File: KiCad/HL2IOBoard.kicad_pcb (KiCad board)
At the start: 4 copper layers, 93 x 53.4 mm, 117 parts, among them J1 Conn_02x25_Odd_Even, J10 142-0701-851, J12 Conn_02x01, J2 Conn_01x05, J3 FAN, J4 Conn_02x04_Odd_Even, J5 LD09P13A4GX00LF, J6 Conn_02x04_Odd_Even, J7 Conn_01x09, J8 Conn_01x05, J9 142-0701-851, P1 TestPoint, P2 TestPoint, P3 TestPoint, P4 TestPoint, Q1 NUD3160LT1G, Q2 SSM3J374R,LF, Q3 SSM3J374R,LF, Q4 BC847C-13-F, Q5 BC847C-13-F, Q6 FCX491ATA, Sw12 TestPoint, Sw5 TestPoint, T1 TestPoint, T2 TestPoint, T4 TestPoint, T5 TestPoint, T6 TestPoint, U1 Pico, U11 PCA9536D, U13 TLV9351IDCKR, U2 MASWSS0179TR-3000, U3 MASWSS0179TR-3000, U4 MASWSS0179TR-3000, U5 AS78L05RTR-E1, U6 MC74HCT04ADR2G, U7 74HCT541PW,118, U8 TBD62381AFNG,EL, U9 LM4040DIM3X-3.0/NOPB

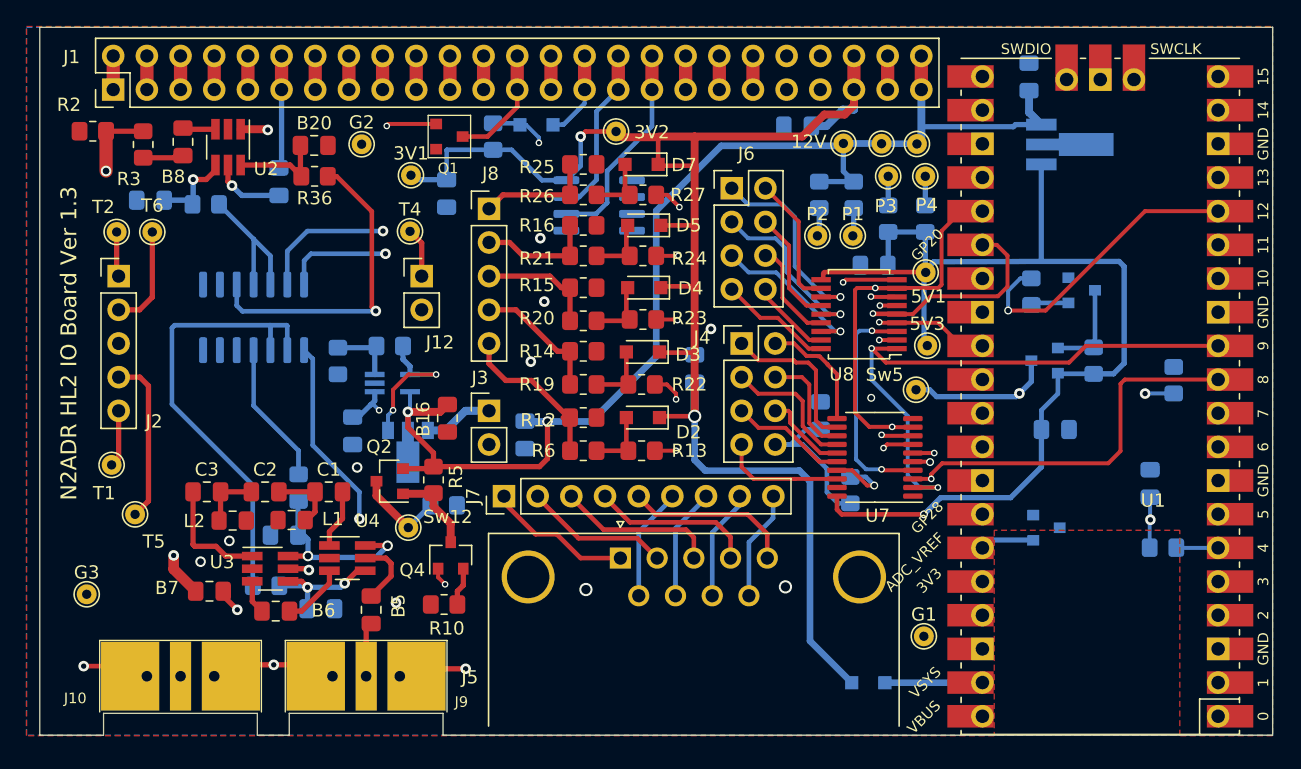
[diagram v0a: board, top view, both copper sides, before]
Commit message: Change the PCB to version 1.4 (Rev E) to replace the unavailable SSOP part with the SOIC TBD62381AFWG,EL.
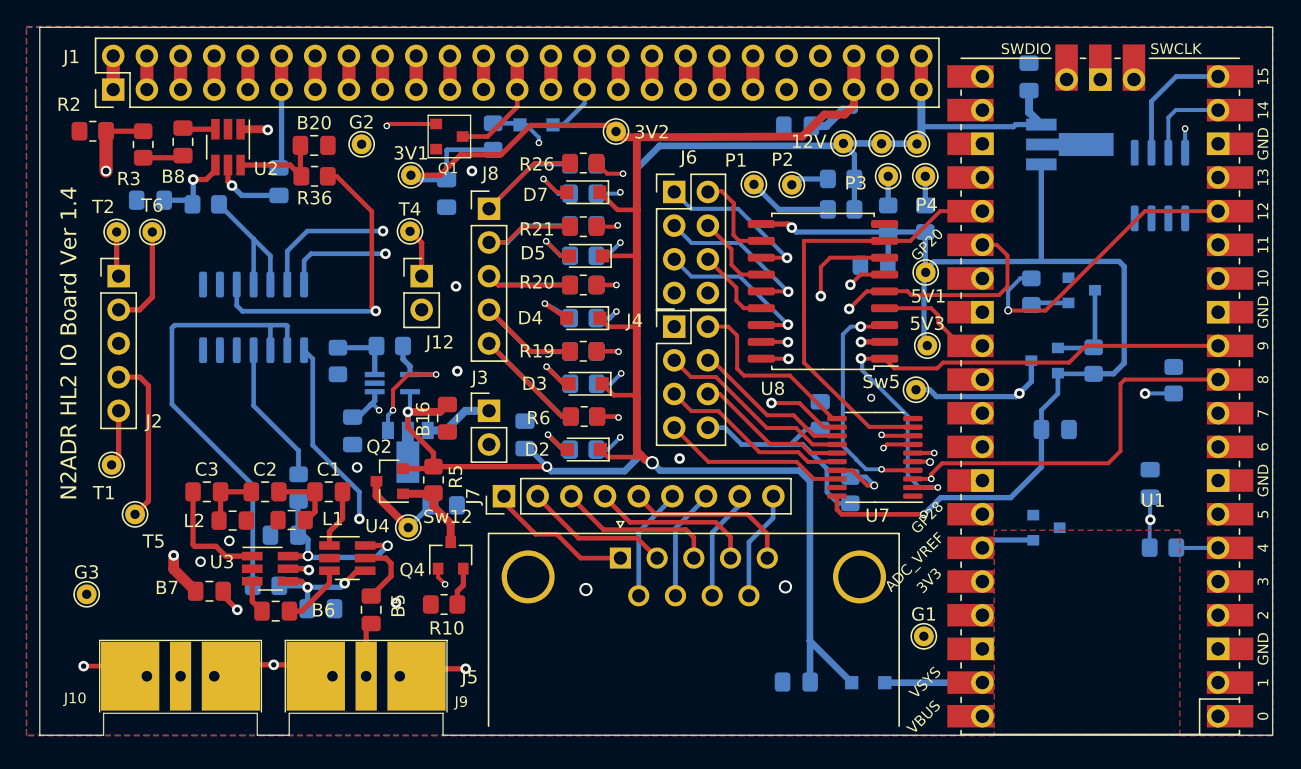
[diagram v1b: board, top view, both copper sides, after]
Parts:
- R12, R13, R14, R15, R16, R22, R23, R24, R25, R27: moved to B.Cu
- U8: value TBD62381AFNG,EL -> TBD62381AFWG,EL; footprint Local:SSOP-18_4.4x6.5mm_P0.65mm -> Package_SO:SOIC-18W_7.5x11.6mm_P1.27mm
- moved U11 42.3 mm to (186.5, 93.5), turned to 90 degrees
- moved B12 24.9 mm to (159.1, 130.9), turned to 0 degrees
- moved P1 8.41 mm to (155.9, 93.4)
- moved J4 5.24 mm to (149.9, 104.1)
- moved D4 5.14 mm to (143.0, 103.5)
- moved D2 5.07 mm to (143.0, 113.4)
- moved D5 4.96 mm to (143.2, 98.8)
- moved D3 4.94 mm to (143.2, 108.5)
- moved D7 4.88 mm to (143.0, 94.0)
- moved R23 4.50 mm to (143.0, 103.5)
- moved R27 4.50 mm to (143.0, 94.1)
- moved R24 4.50 mm to (143.0, 98.8)
- moved R13 4.41 mm to (143.0, 113.4)
- moved R22 4.38 mm to (143.0, 108.5)
- moved J6 4.35 mm to (149.9, 94.0)
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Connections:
- J1 pad 41: Net-(J1-Pad41) -> unconnected-(J1-Pad41)
- J1 pad 42: Net-(J1-Pad42) -> unconnected-(J1-Pad42)
- J1 pad 43: Net-(J1-Pad43) -> unconnected-(J1-Pad43)
- J1 pad 44: Net-(J1-Pad44) -> unconnected-(J1-Pad44)
- U1 pad 30: Net-(U1-Pad30) -> unconnected-(U1-Pad30)
- U1 pad 31: Net-(U1-Pad31) -> unconnected-(U1-Pad31)
- U1 pad 32: Net-(U1-Pad32) -> unconnected-(U1-Pad32)
- U1 pad 34: Net-(U1-Pad34) -> unconnected-(U1-Pad34)
- U1 pad 36: Net-(U1-Pad36) -> unconnected-(U1-Pad36)
- U1 pad 37: Net-(U1-Pad37) -> unconnected-(U1-Pad37)
- U1 pad 40: Net-(U1-Pad40) -> unconnected-(U1-Pad40)
- U1 pad 41: Net-(U1-Pad41) -> unconnected-(U1-Pad41)
- U1 pad 43: Net-(U1-Pad43) -> unconnected-(U1-Pad43)
- U1 pad 7: Net-(U1-Pad7) -> unconnected-(U1-Pad7)
- U11 pad 1: Net-(U11-Pad1) -> unconnected-(U11-Pad1)
- U6 pad 6: Net-(U6-Pad6) -> unconnected-(U6-Pad6)
- U6 pad 8: Net-(U6-Pad8) -> unconnected-(U6-Pad8)
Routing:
- net +3V3: track 119.4 -> 161.5 mm
- net Out1: track 47.7 -> 57.2 mm
- net Net-(D7-Pad2): track 4.84 -> 13.1 mm, vias 0 -> 2
- net +5V: track 132.4 -> 125.1 mm, vias 2 -> 3
- net Net-(D3-Pad2): track 4.86 -> 12.1 mm, vias 0 -> 2
- net Net-(D5-Pad2): track 4.90 -> 12.0 mm, vias 0 -> 2
- net Net-(D2-Pad2): track 5.06 -> 11.5 mm, vias 0 -> 2
- net Net-(D4-Pad2): track 5.14 -> 11.4 mm, vias 0 -> 2
- net Net-(J8-Pad1): track 8.84 -> 15.0 mm
- net In4: track 51.2 -> 57.1 mm
- net In5: track 45.5 -> 51.2 mm
- net Out4: track 44.6 -> 50.3 mm
- net Net-(J4-Pad5): track 8.79 -> 14.4 mm
- net Net-(C5-Pad1): track 12.4 -> 18.0 mm
- net Net-(J4-Pad2): track 9.00 -> 14.1 mm
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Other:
- net class Default removed
- board text added: "N2ADR HL2 IO Board Ver 1.4"
- board text removed: "N2ADR HL2 IO Board Ver 1.3"

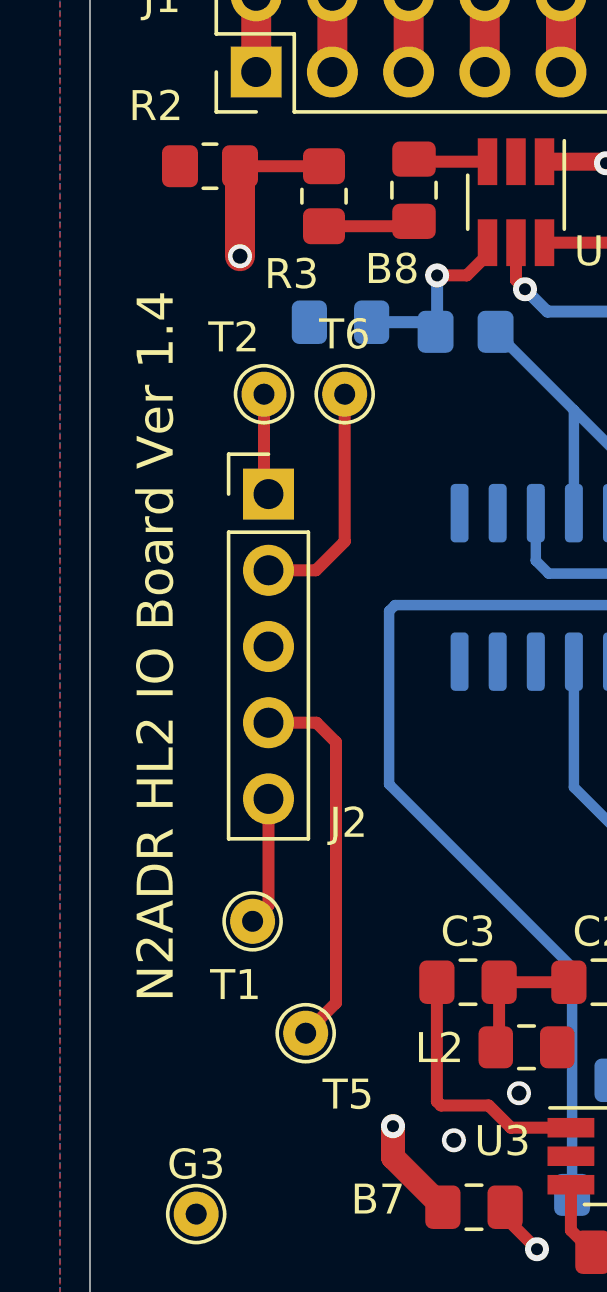
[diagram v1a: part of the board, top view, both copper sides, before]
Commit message: Add the IO board control program.
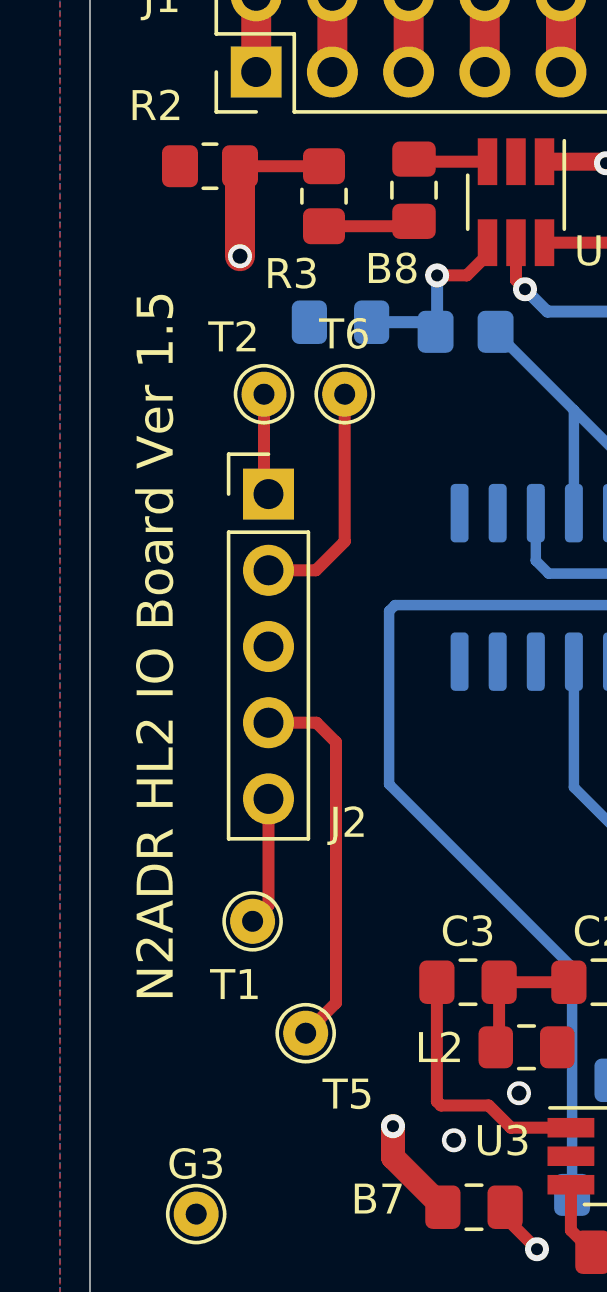
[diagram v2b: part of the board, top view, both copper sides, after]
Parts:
- C2: value 1500p -> 680p
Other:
- board text added: "N2ADR HL2 IO Board Ver 1.5"
- board text removed: "N2ADR HL2 IO Board Ver 1.4"
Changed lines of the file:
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@@
   (title_block
     (title "Hermes Lite2 IO Connector")
-    (date "2023-03-26")
-    (rev "E")
+    (date "2023-09-12")
+    (rev "F")
     (company "N2ADR")
   )
@@
       (effects (font (size 1 1) (thickness 0.15)))
     )
-    (fp_text value "1500p" (at 0 1.68) (layer "F.Fab")
+    (fp_text value "680p" (at 0 1.68) (layer "F.Fab")
       (effects (font (size 1 1) (thickness 0.15)))
     )
@@
   (gr_line (start 102 81.56) (end 195 81.56) (layer "Edge.Cuts") (width 0.05))
   (gr_line (start 195 81.56) (end 195 134.96) (layer "Edge.Cuts") (width 0.05))
-  (gr_text "N2ADR HL2 IO Board Ver 1.4" (at 104.2 105.4 90) (layer "F.SilkS")
+  (gr_text "N2ADR HL2 IO Board Ver 1.5" (at 104.2 105.4 90) (layer "F.SilkS")
     (effects (font (size 1.2 1.2) (thickness 0.15)))
   )

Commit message: Change to PCB.
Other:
- board text added: "N2ADR HL2 IO Board Ver 1.4"
- board text removed: "N2ADR HL2 IO Board Ver 1.5"
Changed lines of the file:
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@@
   (gr_line (start 102 81.56) (end 195 81.56) (layer "Edge.Cuts") (width 0.05))
   (gr_line (start 195 81.56) (end 195 134.96) (layer "Edge.Cuts") (width 0.05))
-  (gr_text "N2ADR HL2 IO Board Ver 1.5" (at 104.2 105.4 90) (layer "F.SilkS")
+  (gr_text "N2ADR HL2 IO Board Ver 1.4" (at 104.2 105.4 90) (layer "F.SilkS")
     (effects (font (size 1.2 1.2) (thickness 0.15)))
   )
